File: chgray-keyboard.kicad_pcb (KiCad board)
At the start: 2 copper layers, 377.4 x 105.5 mm, 175 parts, among them SW1 30, SW10 22, SW11 32, SW12 52, SW13 02, SW14 12, SW15 03, SW16 13, SW17 23, SW18 33, SW19 43, SW2 40, SW20 53, SW21 24, SW22 34, SW23 54, SW24 04, SW25 14, SW26 05, SW27 15, SW28 25, SW29 35, SW3 50, SW30 45, SW31 26, SW32 36, SW33 46, SW34 56, SW35 06, SW36 16, SW37 07, SW38 17, SW39 27, SW4 00, SW40 37, SW41 57, SW42 28, SW43 38, SW44 48, SW45 58, SW46 08, SW47 18, SW48 09, SW49 19, SW5 01, SW50 29, SW51 39, SW52 49, SW53 010, SW54 110, SW55 210, SW56 310, SW57 410, SW58 510, SW59 111, SW6 11, SW60 211, SW61 311, SW62 411, SW63 511, SW64 111, SW65 211, SW66 311, SW67 411, SW68 511, SW69 111, SW7 21, SW70 211, SW71 311, SW72 411, SW73 511, SW8 41, SW9 51, U1 Teensy2.0_(C)

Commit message: placed LED's ..mostly
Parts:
- added C10: C, Capacitor_SMD:C_0402_1005Metric, F.Cu at (128.0, 72.4)
- added C11: C, Capacitor_SMD:C_0402_1005Metric, F.Cu at (133.3, 66.2)
- added C12: C, Capacitor_SMD:C_0402_1005Metric, F.Cu at (237.5, 61.6)
- added C13: C, Capacitor_SMD:C_0402_1005Metric, F.Cu at (226.0, 61.6)
- added C14: C, Capacitor_SMD:C_0402_1005Metric, F.Cu at (228.9, 61.6)
- added C15: C, Capacitor_SMD:C_0402_1005Metric, F.Cu at (226.0, 63.6)
- added C16: C, Capacitor_SMD:C_0402_1005Metric, F.Cu at (228.9, 63.6)
- added C17: C, Capacitor_SMD:C_0402_1005Metric, F.Cu at (231.8, 61.6)
- added C18: C, Capacitor_SMD:C_0402_1005Metric, F.Cu at (231.8, 63.6)
- added C19: C, Capacitor_SMD:C_0402_1005Metric, F.Cu at (234.6, 61.6)
- added C20: C, Capacitor_SMD:C_0402_1005Metric, F.Cu at (234.6, 63.6)
- added C21: C, Capacitor_SMD:C_0402_1005Metric, F.Cu at (250.6, 51.5)
- added C22: C, Capacitor_SMD:C_0402_1005Metric, F.Cu at (223.0, 226.6)
- added C23: C, Capacitor_SMD:C_0402_1005Metric, F.Cu at (446.2, 214.0)
- added C24: C, Capacitor_SMD:C_0402_1005Metric, F.Cu at (349.3, 212.5)
- added C25: C, Capacitor_SMD:C_0402_1005Metric, F.Cu at (346.8, 214.4)
- added C26: C, Capacitor_SMD:C_0402_1005Metric, F.Cu at (226.8, 237.1)
- added C27: C, Capacitor_SMD:C_0402_1005Metric, F.Cu at (397.6, 214.0)
- added C28: C, Capacitor_SMD:C_0402_1005Metric, F.Cu at (394.7, 215.9)
- added C29: C, Capacitor_SMD:C_0402_1005Metric, F.Cu at (346.4, 212.5)
- added C30: C, Capacitor_SMD:C_0402_1005Metric, F.Cu at (446.2, 212.1)
- added C31: C, Capacitor_SMD:C_0402_1005Metric, F.Cu at (221.5, 241.2)
- added C32: C, Capacitor_SMD:C_0402_1005Metric, F.Cu at (224.4, 241.2)
- added C33: C, Capacitor_SMD:C_0402_1005Metric, F.Cu at (391.8, 212.0)
- added C34: C, Capacitor_SMD:C_0402_1005Metric, F.Cu at (218.6, 241.2)
- added C35: C, Capacitor_SMD:C_0402_1005Metric, F.Cu at (394.7, 212.0)
- added C36: C, Capacitor_SMD:C_0402_1005Metric, F.Cu at (391.8, 214.0)
- added C37: C, Capacitor_SMD:C_0402_1005Metric, F.Cu at (223.0, 228.5)
- added C38: C, Capacitor_SMD:C_0402_1005Metric, F.Cu at (394.7, 214.0)
- added C39: C, Capacitor_SMD:C_0402_1005Metric, F.Cu at (391.8, 215.9)
- added C4: C, Capacitor_SMD:C_0402_1005Metric, F.Cu at (133.3, 60.3)
- added C40: C, Capacitor_SMD:C_0402_1005Metric, F.Cu at (397.6, 212.0)
- added C41: C, Capacitor_SMD:C_0402_1005Metric, F.Cu at (223.0, 230.5)
- added C42: C, Capacitor_SMD:C_0402_1005Metric, F.Cu at (111.8, 230.9)
- added C43: C, Capacitor_SMD:C_0402_1005Metric, F.Cu at (97.7, 228.5)
- added C44: C, Capacitor_SMD:C_0402_1005Metric, F.Cu at (108.7, 217.6)
- added C45: C, Capacitor_SMD:C_0402_1005Metric, F.Cu at (106.3, 219.5)
- added C46: C, Capacitor_SMD:C_0402_1005Metric, F.Cu at (111.8, 236.8)
- added C47: C, Capacitor_SMD:C_0402_1005Metric, F.Cu at (103.4, 222.6)
- added C48: C, Capacitor_SMD:C_0402_1005Metric, F.Cu at (100.6, 224.6)
- added C49: C, Capacitor_SMD:C_0402_1005Metric, F.Cu at (105.9, 217.6)
- added C5: C, Capacitor_SMD:C_0402_1005Metric, F.Cu at (125.2, 70.4)
- added C50: C, Capacitor_SMD:C_0402_1005Metric, F.Cu at (97.7, 226.5)
- added C51: C, Capacitor_SMD:C_0402_1005Metric, F.Cu at (359.4, 195.8)
- added C52: C, Capacitor_SMD:C_0402_1005Metric, F.Cu at (315.1, 200.6)
- added C53: C, Capacitor_SMD:C_0402_1005Metric, F.Cu at (97.7, 220.6)
- added C54: C, Capacitor_SMD:C_0402_1005Metric, F.Cu at (356.6, 195.8)
- added C55: C, Capacitor_SMD:C_0402_1005Metric, F.Cu at (100.6, 220.6)
- added C56: C, Capacitor_SMD:C_0402_1005Metric, F.Cu at (97.7, 222.6)
- added C57: C, Capacitor_SMD:C_0402_1005Metric, F.Cu at (111.8, 232.9)
- added C58: C, Capacitor_SMD:C_0402_1005Metric, F.Cu at (100.6, 222.6)
- added C59: C, Capacitor_SMD:C_0402_1005Metric, F.Cu at (97.7, 224.6)
- added C6: C, Capacitor_SMD:C_0402_1005Metric, F.Cu at (133.3, 62.3)
- added C60: C, Capacitor_SMD:C_0402_1005Metric, F.Cu at (103.4, 220.6)
- added C61: C, Capacitor_SMD:C_0402_1005Metric, F.Cu at (111.8, 234.8)
- added C62: C, Capacitor_SMD:C_0402_1005Metric, F.Cu at (199.9, 221.2)
- added C63: C, Capacitor_SMD:C_0402_1005Metric, F.Cu at (183.5, 244.3)
- added C64: C, Capacitor_SMD:C_0402_1005Metric, F.Cu at (194.6, 233.3)
- added C65: C, Capacitor_SMD:C_0402_1005Metric, F.Cu at (192.1, 235.3)
- added C66: C, Capacitor_SMD:C_0402_1005Metric, F.Cu at (199.9, 227.1)
- added C67: C, Capacitor_SMD:C_0402_1005Metric, F.Cu at (189.3, 238.4)
- added C68: C, Capacitor_SMD:C_0402_1005Metric, F.Cu at (186.4, 240.3)
- added C69: C, Capacitor_SMD:C_0402_1005Metric, F.Cu at (191.7, 233.3)
- added C7: C, Capacitor_SMD:C_0402_1005Metric, F.Cu at (128.0, 70.4)
- added C70: C, Capacitor_SMD:C_0402_1005Metric, F.Cu at (183.5, 242.3)
- added C71: C, Capacitor_SMD:C_0402_1005Metric, F.Cu at (194.6, 231.3)
- added C72: C, Capacitor_SMD:C_0402_1005Metric, F.Cu at (197.5, 231.3)
- added C73: C, Capacitor_SMD:C_0402_1005Metric, F.Cu at (183.5, 236.4)
- added C74: C, Capacitor_SMD:C_0402_1005Metric, F.Cu at (191.7, 231.3)
- added C75: C, Capacitor_SMD:C_0402_1005Metric, F.Cu at (186.4, 236.4)
- added C76: C, Capacitor_SMD:C_0402_1005Metric, F.Cu at (183.5, 238.4)
- added C77: C, Capacitor_SMD:C_0402_1005Metric, F.Cu at (199.9, 223.2)
- added C78: C, Capacitor_SMD:C_0402_1005Metric, F.Cu at (186.4, 238.4)
- added C79: C, Capacitor_SMD:C_0402_1005Metric, F.Cu at (183.5, 240.3)
- added C8: C, Capacitor_SMD:C_0402_1005Metric, F.Cu at (133.3, 64.3)
- added C80: C, Capacitor_SMD:C_0402_1005Metric, F.Cu at (189.3, 236.4)
- added C81: C, Capacitor_SMD:C_0402_1005Metric, F.Cu at (199.9, 225.2)
- added C82: C, Capacitor_SMD:C_0402_1005Metric, F.Cu at (324.4, 209.6)
- added C83: C, Capacitor_SMD:C_0402_1005Metric, F.Cu at (327.2, 209.6)
- added C9: C, Capacitor_SMD:C_0402_1005Metric, F.Cu at (125.2, 72.4)
- added D100: LED, daprice-keyswitches:LED_SK6812MINI_PLCC4_3.5x3.5mm_P1.75mm, F.Cu at (363.0, 100.9)
- added D101: LED, daprice-keyswitches:LED_SK6812MINI_PLCC4_3.5x3.5mm_P1.75mm, F.Cu at (382.0, 100.6)
- added D102: LED, daprice-keyswitches:LED_SK6812MINI_PLCC4_3.5x3.5mm_P1.75mm, F.Cu at (382.5, 119.4)
- added D103: LED, daprice-keyswitches:LED_SK6812MINI_PLCC4_3.5x3.5mm_P1.75mm, F.Cu at (363.0, 119.6)
- added D104: LED, daprice-keyswitches:LED_SK6812MINI_PLCC4_3.5x3.5mm_P1.75mm, F.Cu at (343.9, 119.6)
- added D105: LED, daprice-keyswitches:LED_SK6812MINI_PLCC4_3.5x3.5mm_P1.75mm, F.Cu at (325.1, 119.7)
- added D106: LED, daprice-keyswitches:LED_SK6812MINI_PLCC4_3.5x3.5mm_P1.75mm, F.Cu at (286.5, 120.1)
- added D107: LED, daprice-keyswitches:LED_SK6812MINI_PLCC4_3.5x3.5mm_P1.75mm, F.Cu at (265.7, 120.1)
- added D108: LED, daprice-keyswitches:LED_SK6812MINI_PLCC4_3.5x3.5mm_P1.75mm, F.Cu at (248.7, 118.9)
- added D109: LED, daprice-keyswitches:LED_SK6812MINI_PLCC4_3.5x3.5mm_P1.75mm, F.Cu at (229.1, 119.4)
- added D110: LED, daprice-keyswitches:LED_SK6812MINI_PLCC4_3.5x3.5mm_P1.75mm, F.Cu at (210.8, 119.6)
- added D111: LED, daprice-keyswitches:LED_SK6812MINI_PLCC4_3.5x3.5mm_P1.75mm, F.Cu at (191.5, 119.5)
- added D112: LED, daprice-keyswitches:LED_SK6812MINI_PLCC4_3.5x3.5mm_P1.75mm, F.Cu at (173.2, 120.1)
- added D113: LED, daprice-keyswitches:LED_SK6812MINI_PLCC4_3.5x3.5mm_P1.75mm, F.Cu at (152.9, 119.9)
- added D114: LED, daprice-keyswitches:LED_SK6812MINI_PLCC4_3.5x3.5mm_P1.75mm, F.Cu at (133.9, 120.7)
- added D115: LED, daprice-keyswitches:LED_SK6812MINI_PLCC4_3.5x3.5mm_P1.75mm, F.Cu at (114.8, 120.1)
- added D116: LED, daprice-keyswitches:LED_SK6812MINI_PLCC4_3.5x3.5mm_P1.75mm, F.Cu at (95.2, 120.1)
- added D117: LED, daprice-keyswitches:LED_SK6812MINI_PLCC4_3.5x3.5mm_P1.75mm, F.Cu at (77.5, 120.2)
- added D118: LED, daprice-keyswitches:LED_SK6812MINI_PLCC4_3.5x3.5mm_P1.75mm, F.Cu at (58.4, 121.4)
- added D119: LED, daprice-keyswitches:LED_SK6812MINI_PLCC4_3.5x3.5mm_P1.75mm, F.Cu at (36.3, 120.1)
- added D120: LED, daprice-keyswitches:LED_SK6812MINI_PLCC4_3.5x3.5mm_P1.75mm, F.Cu at (38.9, 137.9)
- added D121: LED, daprice-keyswitches:LED_SK6812MINI_PLCC4_3.5x3.5mm_P1.75mm, F.Cu at (62.2, 138.4)
- added D122: LED, daprice-keyswitches:LED_SK6812MINI_PLCC4_3.5x3.5mm_P1.75mm, F.Cu at (82.0, 138.5)
- added D123: LED, daprice-keyswitches:LED_SK6812MINI_PLCC4_3.5x3.5mm_P1.75mm, F.Cu at (100.8, 138.2)
- added D124: LED, daprice-keyswitches:LED_SK6812MINI_PLCC4_3.5x3.5mm_P1.75mm, F.Cu at (120.1, 138.8)
- added D125: LED, daprice-keyswitches:LED_SK6812MINI_PLCC4_3.5x3.5mm_P1.75mm, F.Cu at (138.9, 138.7)
- added D126: LED, daprice-keyswitches:LED_SK6812MINI_PLCC4_3.5x3.5mm_P1.75mm, F.Cu at (158.0, 139.2)
- added D127: LED, daprice-keyswitches:LED_SK6812MINI_PLCC4_3.5x3.5mm_P1.75mm, F.Cu at (176.5, 139.7)
- added D128: LED, daprice-keyswitches:LED_SK6812MINI_PLCC4_3.5x3.5mm_P1.75mm, F.Cu at (195.8, 140.2)
- added D129: LED, daprice-keyswitches:LED_SK6812MINI_PLCC4_3.5x3.5mm_P1.75mm, F.Cu at (215.4, 140.2)
- added D130: LED, daprice-keyswitches:LED_SK6812MINI_PLCC4_3.5x3.5mm_P1.75mm, F.Cu at (234.4, 139.8)
- added D131: LED, daprice-keyswitches:LED_SK6812MINI_PLCC4_3.5x3.5mm_P1.75mm, F.Cu at (253.5, 139.4)
- added D132: LED, daprice-keyswitches:LED_SK6812MINI_PLCC4_3.5x3.5mm_P1.75mm, F.Cu at (279.1, 139.2)
- added D133: LED, daprice-keyswitches:LED_SK6812MINI_PLCC4_3.5x3.5mm_P1.75mm, F.Cu at (324.6, 139.5)
- added D134: LED, daprice-keyswitches:LED_SK6812MINI_PLCC4_3.5x3.5mm_P1.75mm, F.Cu at (344.2, 140.2)
- added D135: LED, daprice-keyswitches:LED_SK6812MINI_PLCC4_3.5x3.5mm_P1.75mm, F.Cu at (363.0, 140.2)
- added D136: LED, daprice-keyswitches:LED_SK6812MINI_PLCC4_3.5x3.5mm_P1.75mm, F.Cu at (382.5, 140.0)
- added D137: LED, daprice-keyswitches:LED_SK6812MINI_PLCC4_3.5x3.5mm_P1.75mm, F.Cu at (381.8, 158.2)
- added D138: LED, daprice-keyswitches:LED_SK6812MINI_PLCC4_3.5x3.5mm_P1.75mm, F.Cu at (363.5, 158.3)
- added D139: LED, daprice-keyswitches:LED_SK6812MINI_PLCC4_3.5x3.5mm_P1.75mm, F.Cu at (343.9, 158.8)
- added D140: LED, daprice-keyswitches:LED_SK6812MINI_PLCC4_3.5x3.5mm_P1.75mm, F.Cu at (325.4, 159.0)
- added D141: LED, daprice-keyswitches:LED_SK6812MINI_PLCC4_3.5x3.5mm_P1.75mm, F.Cu at (274.8, 157.9)
- added D142: LED, daprice-keyswitches:LED_SK6812MINI_PLCC4_3.5x3.5mm_P1.75mm, F.Cu at (243.6, 158.0)
- added D143: LED, daprice-keyswitches:LED_SK6812MINI_PLCC4_3.5x3.5mm_P1.75mm, F.Cu at (225.3, 158.8)
- added D144: LED, daprice-keyswitches:LED_SK6812MINI_PLCC4_3.5x3.5mm_P1.75mm, F.Cu at (206.0, 158.6)
- added D145: LED, daprice-keyswitches:LED_SK6812MINI_PLCC4_3.5x3.5mm_P1.75mm, F.Cu at (186.9, 158.0)
- added D146: LED, daprice-keyswitches:LED_SK6812MINI_PLCC4_3.5x3.5mm_P1.75mm, F.Cu at (167.6, 159.0)
- added D147: LED, daprice-keyswitches:LED_SK6812MINI_PLCC4_3.5x3.5mm_P1.75mm, F.Cu at (149.1, 159.0)
- added D148: LED, daprice-keyswitches:LED_SK6812MINI_PLCC4_3.5x3.5mm_P1.75mm, F.Cu at (130.3, 159.0)
- added D149: LED, daprice-keyswitches:LED_SK6812MINI_PLCC4_3.5x3.5mm_P1.75mm, F.Cu at (110.5, 158.5)
- added D150: LED, daprice-keyswitches:LED_SK6812MINI_PLCC4_3.5x3.5mm_P1.75mm, F.Cu at (92.5, 158.5)
- added D151: LED, daprice-keyswitches:LED_SK6812MINI_PLCC4_3.5x3.5mm_P1.75mm, F.Cu at (72.9, 158.2)
- added D152: LED, daprice-keyswitches:LED_SK6812MINI_PLCC4_3.5x3.5mm_P1.75mm, F.Cu at (43.9, 158.1)
- added D153: LED, daprice-keyswitches:LED_SK6812MINI_PLCC4_3.5x3.5mm_P1.75mm, F.Cu at (34.5, 177.8)
- added D154: LED, daprice-keyswitches:LED_SK6812MINI_PLCC4_3.5x3.5mm_P1.75mm, F.Cu at (53.1, 177.5)
- added D155: LED, daprice-keyswitches:LED_SK6812MINI_PLCC4_3.5x3.5mm_P1.75mm, F.Cu at (77.2, 177.0)
- added D156: LED, daprice-keyswitches:LED_SK6812MINI_PLCC4_3.5x3.5mm_P1.75mm, F.Cu at (100.8, 177.5)
- added D157: LED, daprice-keyswitches:LED_SK6812MINI_PLCC4_3.5x3.5mm_P1.75mm, F.Cu at (131.6, 177.5)
- added D158: LED, daprice-keyswitches:LED_SK6812MINI_PLCC4_3.5x3.5mm_P1.75mm, F.Cu at (162.6, 177.8)
- added D159: LED, daprice-keyswitches:LED_SK6812MINI_PLCC4_3.5x3.5mm_P1.75mm, F.Cu at (181.6, 177.8)
- added D160: LED, daprice-keyswitches:LED_SK6812MINI_PLCC4_3.5x3.5mm_P1.75mm, F.Cu at (212.9, 177.5)
- added D161: LED, daprice-keyswitches:LED_SK6812MINI_PLCC4_3.5x3.5mm_P1.75mm, F.Cu at (245.9, 177.8)
- added D162: LED, daprice-keyswitches:LED_SK6812MINI_PLCC4_3.5x3.5mm_P1.75mm, F.Cu at (268.5, 177.5)
- added D163: LED, daprice-keyswitches:LED_SK6812MINI_PLCC4_3.5x3.5mm_P1.75mm, F.Cu at (286.8, 177.5)
- added D164: LED, daprice-keyswitches:LED_SK6812MINI_PLCC4_3.5x3.5mm_P1.75mm, F.Cu at (324.9, 177.0)
- added D165: LED, daprice-keyswitches:LED_SK6812MINI_PLCC4_3.5x3.5mm_P1.75mm, F.Cu at (344.2, 177.0)
- added D166: LED, daprice-keyswitches:LED_SK6812MINI_PLCC4_3.5x3.5mm_P1.75mm, F.Cu at (363.0, 177.5)
- added D167: LED, daprice-keyswitches:LED_SK6812MINI_PLCC4_3.5x3.5mm_P1.75mm, F.Cu at (382.0, 176.8)
- added D88: LED, daprice-keyswitches:LED_SK6812MINI_PLCC4_3.5x3.5mm_P1.75mm, F.Cu at (91.4, 100.3)
- added D89: LED, daprice-keyswitches:LED_SK6812MINI_PLCC4_3.5x3.5mm_P1.75mm, F.Cu at (110.5, 100.3)
- added D90: LED, daprice-keyswitches:LED_SK6812MINI_PLCC4_3.5x3.5mm_P1.75mm, F.Cu at (129.3, 100.3)
- added D91: LED, daprice-keyswitches:LED_SK6812MINI_PLCC4_3.5x3.5mm_P1.75mm, F.Cu at (148.1, 100.3)
- added D92: LED, daprice-keyswitches:LED_SK6812MINI_PLCC4_3.5x3.5mm_P1.75mm, F.Cu at (167.9, 100.6)
- added D93: LED, daprice-keyswitches:LED_SK6812MINI_PLCC4_3.5x3.5mm_P1.75mm, F.Cu at (186.7, 100.3)
- added D94: LED, daprice-keyswitches:LED_SK6812MINI_PLCC4_3.5x3.5mm_P1.75mm, F.Cu at (205.7, 100.3)
- added D95: LED, daprice-keyswitches:LED_SK6812MINI_PLCC4_3.5x3.5mm_P1.75mm, F.Cu at (224.8, 100.3)
- added D96: LED, daprice-keyswitches:LED_SK6812MINI_PLCC4_3.5x3.5mm_P1.75mm, F.Cu at (243.6, 100.3)
- added D97: LED, daprice-keyswitches:LED_SK6812MINI_PLCC4_3.5x3.5mm_P1.75mm, F.Cu at (262.6, 100.3)
- added D98: LED, daprice-keyswitches:LED_SK6812MINI_PLCC4_3.5x3.5mm_P1.75mm, F.Cu at (325.1, 100.6)
- added D99: LED, daprice-keyswitches:LED_SK6812MINI_PLCC4_3.5x3.5mm_P1.75mm, F.Cu at (343.9, 100.4)
- moved D85 247.3 mm to (34.0, 100.1)
- moved D87 227.7 mm to (72.1, 100.4)
- moved D86 227.7 mm to (53.1, 100.3)
- moved C2 182.3 mm to (170.1, 59.7)
- moved C3 182.3 mm to (170.1, 54.6)
- moved C1 173.3 mm to (170.8, 64.1)
- renumbered C4 to C2, C7 to C3, D88 to D86, D91 to D87, S2 to S1, S3 to S2
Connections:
- D85 pad 2: Net-(D85-Pad2) -> (no net)
- D86 pad 4: Net-(D85-Pad2) -> (no net)
- D87 pad 2: (no net) -> Net-(D87-Pad2)
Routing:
- net /Keyboard Keys/KEY_ROW3: track 592.9 -> 0.00 mm
- net /Keyboard Keys/KEY_ROW4: track 584.7 -> 0.00 mm, vias 6 -> 0
- net /Keyboard Keys/KEY_ROW0: track 488.2 -> 0.00 mm, vias 2 -> 0
- net /Keyboard Keys/KEY_ROW2: track 452.5 -> 0.00 mm, vias 3 -> 0
- net /Keyboard Keys/KEY_ROW1: track 426.7 -> 0.00 mm, vias 3 -> 0
- net /Keyboard Keys/KEY_COL13: track 403.2 -> 0.00 mm, vias 1 -> 0
- net /Keyboard Keys/KEY_ROW5: track 393.7 -> 0.00 mm, vias 5 -> 0
- net /Keyboard Keys/KEY_COL0: track 380.2 -> 0.00 mm, vias 7 -> 0
- net /Keyboard Keys/KEY_COL2: track 361.5 -> 0.00 mm, vias 3 -> 0
- net /Keyboard Keys/KEY_COL1: track 347.0 -> 0.00 mm, vias 4 -> 0
- net Net-(D2-Pad1): track 325.8 -> 0.00 mm, vias 2 -> 0
- net Net-(D83-Pad1): track 321.8 -> 0.00 mm, vias 2 -> 0
- net Net-(D82-Pad1): track 316.5 -> 0.00 mm, vias 2 -> 0
- net /Keyboard Keys/KEY_COL3: track 294.8 -> 0.00 mm, vias 4 -> 0
- net /Keyboard Keys/KEY_COL5: track 289.6 -> 0.00 mm, vias 5 -> 0
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
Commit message: placed LED's ..mostly
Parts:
- added C84: C, Capacitor_SMD:C_0402_1005Metric, B.Cu at (300.1, 157.4)
- added D168: LED, daprice-keyswitches:LED_SK6812MINI_PLCC4_3.5x3.5mm_P1.75mm, F.Cu at (284.1, 100.5)
- C10, C11, C12, C13, C14, C15, C16, C17, C18, C19, C20, C21, C22, C23, C24, C25, C26, C27, C28, C29, C30, C31, C32, C33, C34, C35, C36, C37, C38, C39, C4, C40, C41, C42, C43, C44, C45, C46, C47, C48, C49, C5, C50, C51, C52, C53, C54, C55, C56, C57, C58, C59, C6, C60, C61, C62, C63, C64, C65, C66, C67, C68, C69, C7, C70, C71, C72, C73, C74, C75, C76, C77, C78, C79, C8, C80, C81, C82, C83, C9: moved to B.Cu
- moved C43 229.0 mm to (300.1, 121.6)
- moved C50 226.3 mm to (300.1, 125.4)
- moved C46 224.9 mm to (300.1, 113.9)
- moved C59 224.2 mm to (300.1, 128.2)
- moved C61 223.3 mm to (300.1, 115.0)
- moved C56 222.7 mm to (300.1, 129.8)
- moved C48 221.9 mm to (300.1, 127.6)
- moved C57 221.6 mm to (300.1, 116.1)
- moved C53 219.5 mm to (300.1, 135.9)
- moved C58 219.4 mm to (300.1, 131.5)
- moved C42 218.9 mm to (300.1, 119.4)
- moved C47 217.0 mm to (300.1, 130.9)
- moved C55 216.4 mm to (300.1, 137.0)
- moved C60 214.4 mm to (300.1, 135.4)
- moved C45 210.4 mm to (300.1, 137.6)
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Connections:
- D167 pad 2: (no net) -> Net-(D167-Pad2)

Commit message: placed LED's ..mostly
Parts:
- moved D107 3.29 mm to (267.6, 119.1)
- moved D116 2.88 mm to (96.1, 119.0)
- moved D112 2.84 mm to (172.4, 119.1)
- moved D110 2.76 mm to (210.4, 119.1)
- moved D115 2.75 mm to (115.2, 119.1)
- moved D113 2.74 mm to (153.3, 119.1)
- moved D114 2.73 mm to (134.2, 119.1)
- moved D117 2.72 mm to (77.1, 119.1)
- moved D106 2.68 mm to (286.6, 119.1)
- moved D119 2.67 mm to (36.4, 119.1)
- moved D111 2.38 mm to (191.4, 119.0)
- moved D109 2.33 mm to (229.5, 119.1)
- moved D108 2.33 mm to (248.5, 119.1)
- moved D118 2.32 mm to (58.0, 119.1)
- moved D129 2.09 mm to (215.0, 138.2)
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
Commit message: placed LED's ..mostly
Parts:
- moved D52 32.1 mm to (311.6, 137.5)
- moved C72 28.9 mm to (298.4, 162.6)
- moved C71 28.2 mm to (298.4, 161.3)
- moved C8 27.4 mm to (298.4, 159.9)
- moved C74 26.6 mm to (298.4, 158.6)
- moved C58 25.8 mm to (298.4, 157.2)
- moved C47 25.0 mm to (298.4, 155.9)
- moved C11 24.2 mm to (298.4, 154.6)
- moved C56 23.4 mm to (298.4, 153.2)
- moved C69 22.6 mm to (298.4, 151.9)
- moved C64 21.9 mm to (298.4, 150.5)
- moved D67 21.2 mm to (311.6, 161.7)
- moved C59 21.1 mm to (298.4, 149.2)
- moved C48 20.3 mm to (298.4, 147.8)
- moved C6 19.6 mm to (304.2, 115.0)
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
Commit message: routed
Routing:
- net LED_VDD: track 0.00 -> 2036.1 mm, vias 0 -> 16
- net /Keyboard Keys/KEY_ROW4: track 0.00 -> 613.3 mm, vias 0 -> 10
- net /Keyboard Keys/KEY_COL0: track 0.00 -> 556.2 mm, vias 0 -> 6
- net /Keyboard Keys/KEY_ROW3: track 0.00 -> 549.4 mm, vias 0 -> 10
- net /Keyboard Keys/KEY_ROW0: track 0.00 -> 521.1 mm, vias 0 -> 4
- net /Keyboard Keys/KEY_ROW5: track 0.00 -> 469.0 mm, vias 0 -> 9
- net /Keyboard Keys/KEY_ROW2: track 0.00 -> 455.8 mm, vias 0 -> 7
- net /Keyboard Keys/KEY_ROW1: track 0.00 -> 448.7 mm, vias 0 -> 8
- net /Keyboard Keys/KEY_COL13: track 0.00 -> 424.0 mm, vias 0 -> 8
- net /Keyboard Keys/KEY_COL2: track 0.00 -> 409.9 mm, vias 0 -> 7
- net Net-(C2-Pad1): track 0.00 -> 405.8 mm
- net /Keyboard Keys/KEY_COL1: track 0.00 -> 370.7 mm, vias 0 -> 6
- net Net-(C61-Pad1): track 0.00 -> 365.2 mm, vias 0 -> 4
- net Net-(D83-Pad1): track 0.00 -> 360.3 mm, vias 0 -> 2
- net Net-(D2-Pad1): track 0.00 -> 360.2 mm, vias 0 -> 2
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
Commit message: keyboard
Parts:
- added J1: Conn_01x01_Female, Connector_PinHeader_1.27mm:PinHeader_2x07_P1.27mm_Vertical, F.Cu at (298.4, 180.3)
- U1: moved to F.Cu
- moved C51 54.1 mm to (307.3, 120.1)
- moved C83 54.1 mm to (307.3, 114.7)
- moved C84 54.1 mm to (307.3, 117.4)
- moved C1 54.1 mm to (307.3, 121.5)
- moved C30 54.1 mm to (307.3, 116.1)
- moved C52 54.1 mm to (307.3, 118.8)
- moved C54 54.1 mm to (307.3, 122.8)
- moved C13 1.42 mm to (302.9, 141.2)
- moved C2 1.42 mm to (302.9, 164.1)
- moved C20 1.42 mm to (302.9, 131.9)
- moved C22 1.42 mm to (302.9, 134.5)
- moved C27 1.42 mm to (302.9, 154.7)
- moved C28 1.42 mm to (302.9, 148.0)
- moved C29 1.42 mm to (302.9, 157.3)
- moved C36 1.42 mm to (302.9, 150.6)
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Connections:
- U1 pad 10: /Keyboard Keys/KEY_COL0 -> Net-(J1-Pad7)
- U1 pad 25: /Sheet6096EA01/INPUT -> Net-(J1-Pad3)
- U1 pad 29: (no net) -> Net-(J1-Pad13)
- U1 pad 8: (no net) -> /Keyboard Keys/KEY_COL0
- U1 pad 9: (no net) -> Net-(J1-Pad5)
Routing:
- net LED_VDD: track 2036.1 -> 0.00 mm, vias 16 -> 0
- net /Keyboard Keys/KEY_ROW4: track 613.3 -> 0.00 mm, vias 10 -> 0
- net /Keyboard Keys/KEY_COL0: track 556.2 -> 0.00 mm, vias 6 -> 0
- net /Keyboard Keys/KEY_ROW3: track 549.4 -> 0.00 mm, vias 10 -> 0
- net /Keyboard Keys/KEY_ROW0: track 521.1 -> 0.00 mm, vias 4 -> 0
- net /Keyboard Keys/KEY_ROW5: track 469.0 -> 0.00 mm, vias 9 -> 0
- net /Keyboard Keys/KEY_ROW2: track 455.8 -> 0.00 mm, vias 7 -> 0
- net /Keyboard Keys/KEY_ROW1: track 448.7 -> 0.00 mm, vias 8 -> 0
- net /Keyboard Keys/KEY_COL13: track 424.0 -> 0.00 mm, vias 8 -> 0
- net /Keyboard Keys/KEY_COL2: track 409.9 -> 0.00 mm, vias 7 -> 0
- net Net-(C2-Pad1): track 405.8 -> 0.00 mm
- net /Keyboard Keys/KEY_COL1: track 370.7 -> 0.00 mm, vias 6 -> 0
- net Net-(C61-Pad1): track 365.2 -> 0.00 mm, vias 4 -> 0
- net Net-(D83-Pad1): track 360.3 -> 0.00 mm, vias 2 -> 0
- net Net-(D2-Pad1): track 360.2 -> 0.00 mm, vias 2 -> 0
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
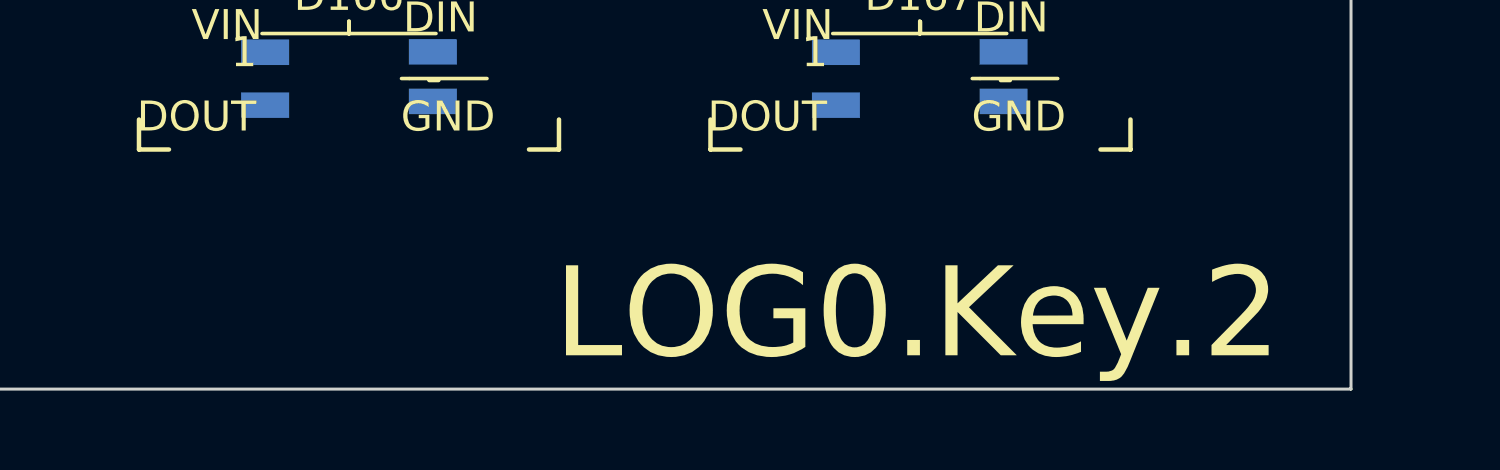
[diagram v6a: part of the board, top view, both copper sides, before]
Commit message: Logan signed off on board location
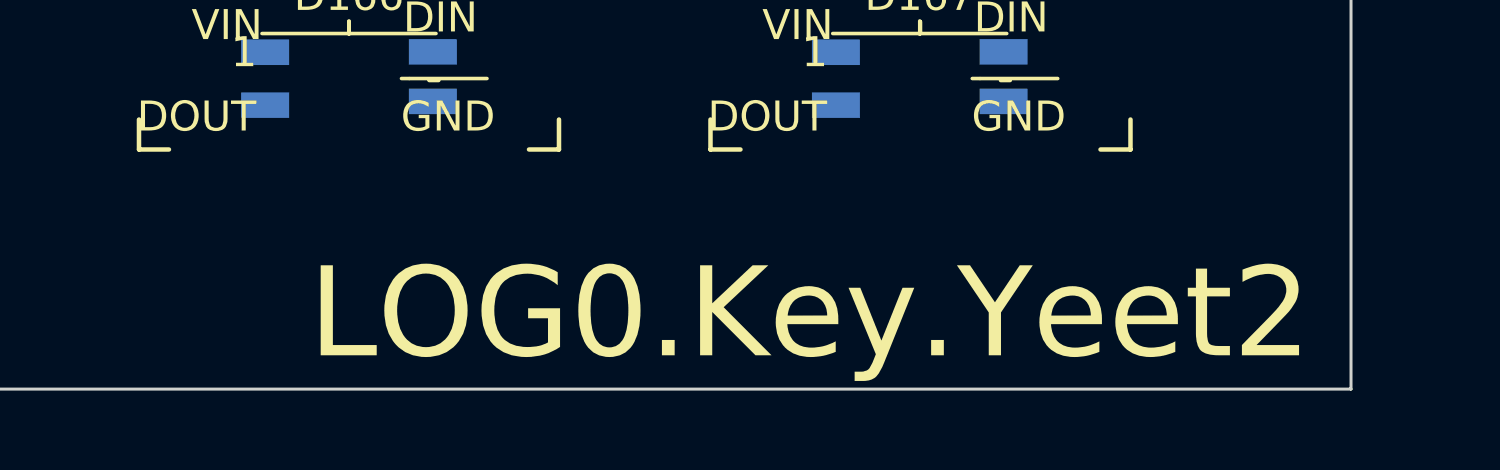
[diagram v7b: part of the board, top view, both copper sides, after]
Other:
- board text added: "LOG0.Key.Yeet2"
- board text removed: "LOG0.Key.2"

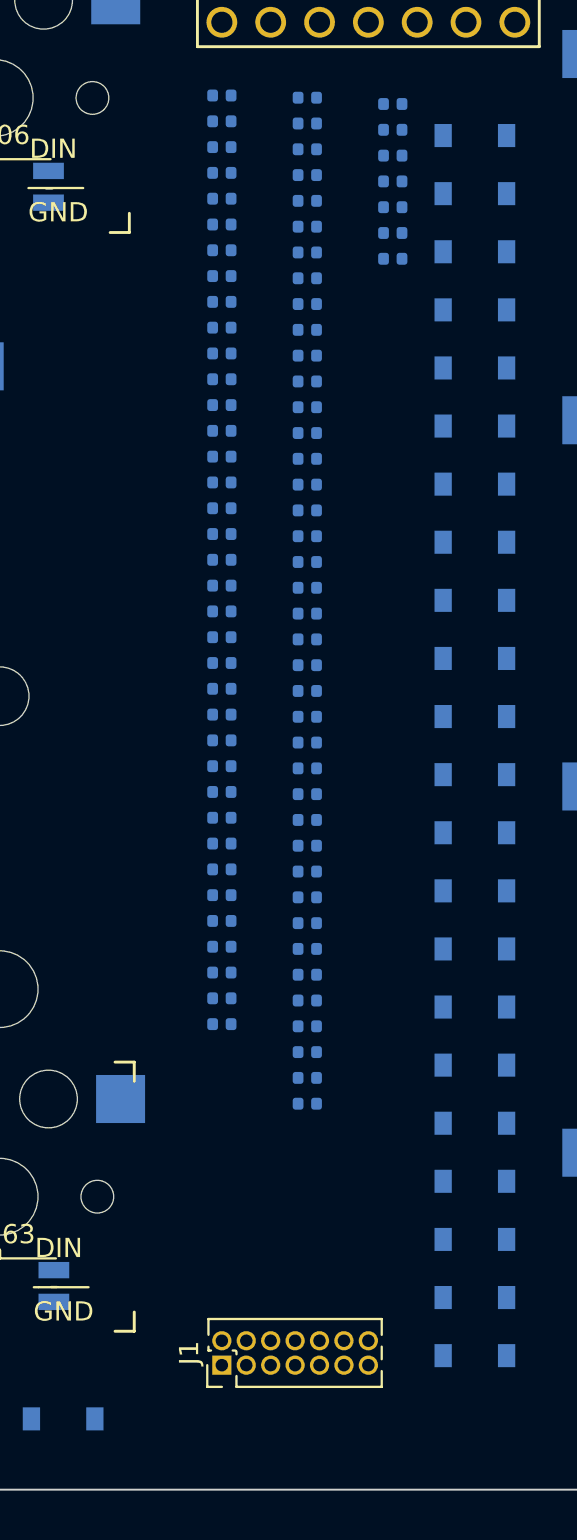
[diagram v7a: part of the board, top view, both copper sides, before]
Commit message: Logan signed off on board location
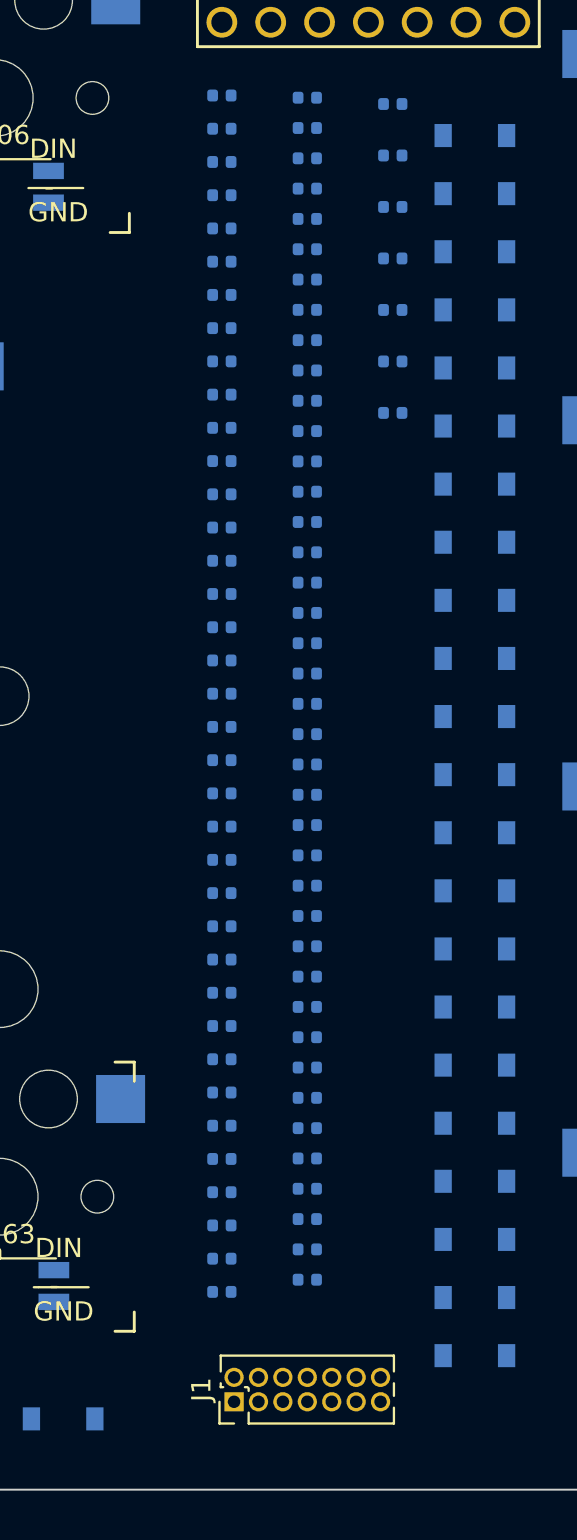
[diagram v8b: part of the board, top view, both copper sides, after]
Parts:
- C1, C10, C11, C12, C13, C14, C15, C16, C17, C18, C19, C2, C20, C21, C22, C23, C24, C25, C26, C27, C28, C29, C3, C30, C31, C32, C33, C34, C35, C36, C37, C38, C39, C4, C40, C41, C42, C43, C44, C45, C46, C47, C48, C49, C5, C50, C51, C52, C53, C54, C55, C56, C57, C58, C59, C6, C60, C61, C62, C63, C64, C65, C66, C67, C68, C69, C7, C70, C71, C72, C73, C74, C75, C76, C77, C78, C79, C8, C80, C81, C82, C83, C84, C9: value C -> C104 0.1uF 100nF
- moved C72 13.9 mm to (298.4, 176.5)
- moved C71 13.5 mm to (298.4, 174.8)
- moved C8 13.2 mm to (298.4, 173.1)
- moved C74 12.8 mm to (298.4, 171.3)
- moved C58 12.4 mm to (298.4, 169.6)
- moved C47 12.0 mm to (298.4, 167.9)
- moved C11 11.6 mm to (298.4, 166.2)
- moved C56 11.2 mm to (298.4, 164.4)
- moved C69 10.8 mm to (298.4, 162.7)
- moved C64 10.4 mm to (298.4, 161.0)
- moved C59 10.1 mm to (298.4, 159.2)
- moved C48 9.67 mm to (298.4, 157.5)
- moved C65 9.29 mm to (298.4, 155.8)
- moved C82 9.15 mm to (302.9, 175.9)
- moved C21 8.92 mm to (302.9, 174.3)
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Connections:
- D85 pad 2: (no net) -> Net-(D85-Pad2)
- D86 pad 4: (no net) -> Net-(D85-Pad2)
